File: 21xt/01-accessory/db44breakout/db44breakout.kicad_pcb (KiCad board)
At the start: 4 copper layers, 53.2 x 28 mm, 13 parts, among them J1 Conn_01x44_Socket, J10 Conn_01x05, J2 Conn_01x05, J3 Conn_01x05, J4 Conn_01x07, J5 Conn_01x05, J6 Conn_01x05, J7 Conn_01x05, J8 Conn_01x05, J9 Conn_01x05

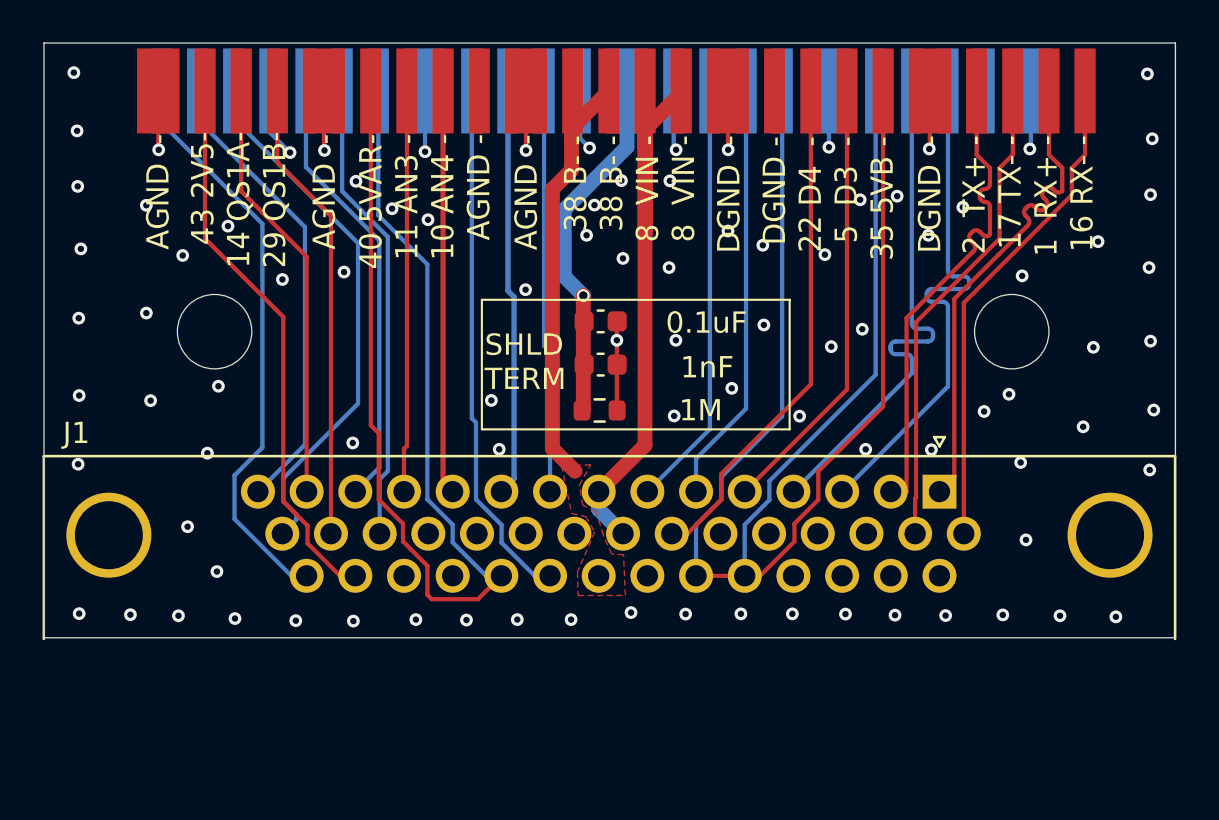
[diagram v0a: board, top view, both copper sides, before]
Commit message: db44 footprint
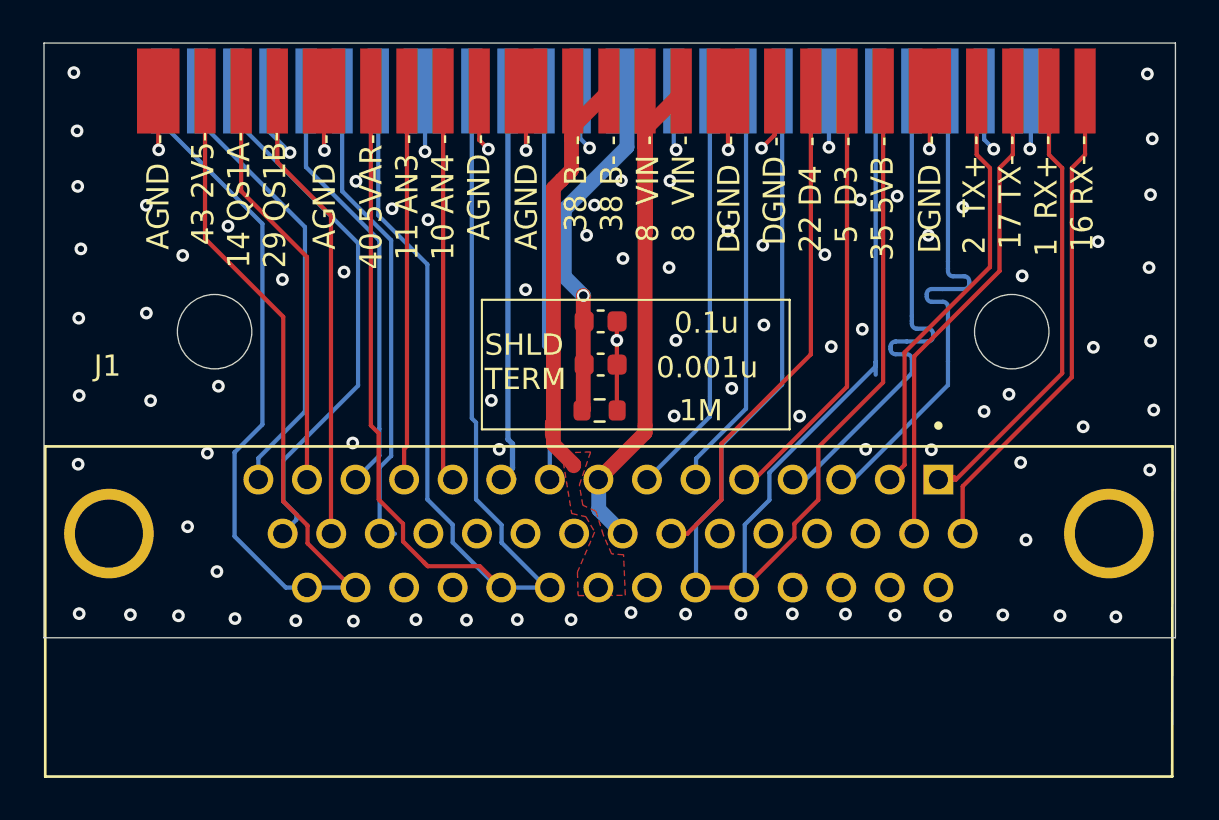
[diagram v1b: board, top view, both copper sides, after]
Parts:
- C1: value 0.1uF -> 0.1u
- C2: value 1nF -> 0.001u
- J1: footprint Connector_Dsub:DSUB-44-HD_Female_Horizontal_P2.29x1.98mm_EdgePinOffset3.03mm_Housed_MountingHolesOffset4.94mm -> 21xt_footprints:AMPHENOL_ICD44S13E4GX00LF
- moved J1 15.7 mm to (185.3, 77.7)
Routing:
- net DGND: track 18.6 -> 24.5 mm, vias 51 -> 53
- net 2V5AR: track 53.3 -> 56.5 mm
- net AGND: track 21.4 -> 24.4 mm, vias 43 -> 44
- net TX+: track 22.9 -> 20.5 mm
- net 5VBuck: track 78.1 -> 78.8 mm
- net 5VAR: track 79.9 -> 80.7 mm
- net RX+: track 23.1 -> 22.4 mm
- net QS2A-: track 21.9 -> 21.3 mm
- net AN1: track 20.7 -> 20.2 mm
- net AN2: track 18.9 -> 18.3 mm
- net QS1A-: track 20.1 -> 19.6 mm
- net VIN: track 30.5 -> 29.9 mm
- net D1: track 20.1 -> 19.5 mm
